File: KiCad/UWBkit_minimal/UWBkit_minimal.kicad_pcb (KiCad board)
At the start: 2 copper layers, 49 x 39.1 mm, 57 parts, among them J1 Conn_UART, J2 Conn_SWD, J3 USB_C_Receptacle_USB2.0_14P, J4 Conn_BATT, J5 Jumper_Cell_NO, Q1 BSS138, Q2 BSS138, Q3 BSS84, SW1 SW_Push, U1 DWM3001C, U2 IP4234CZ6, U3 MAX40203AUK+T, U4 XC9285B33CMR-G

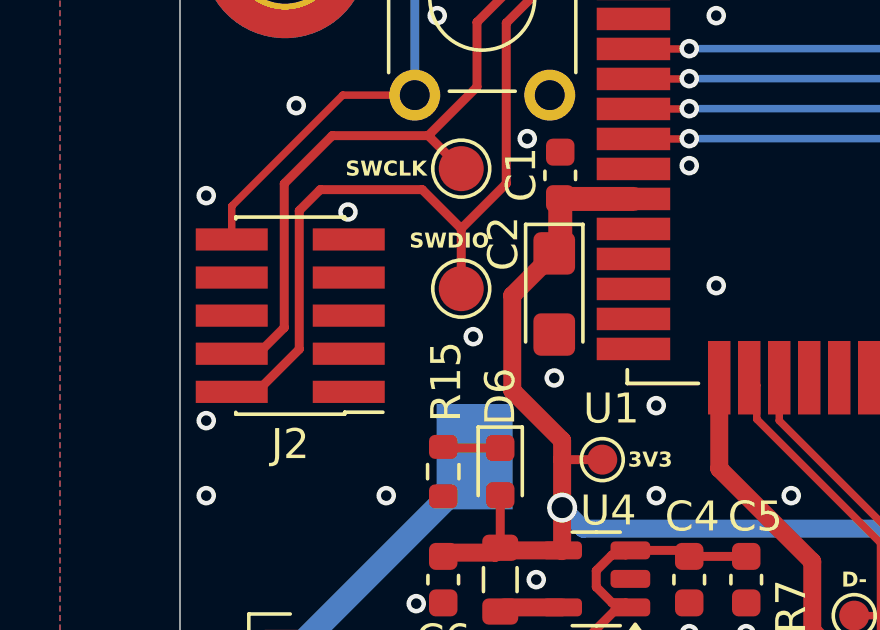
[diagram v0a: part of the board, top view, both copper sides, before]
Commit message: Fixed a missing connection to JTAG
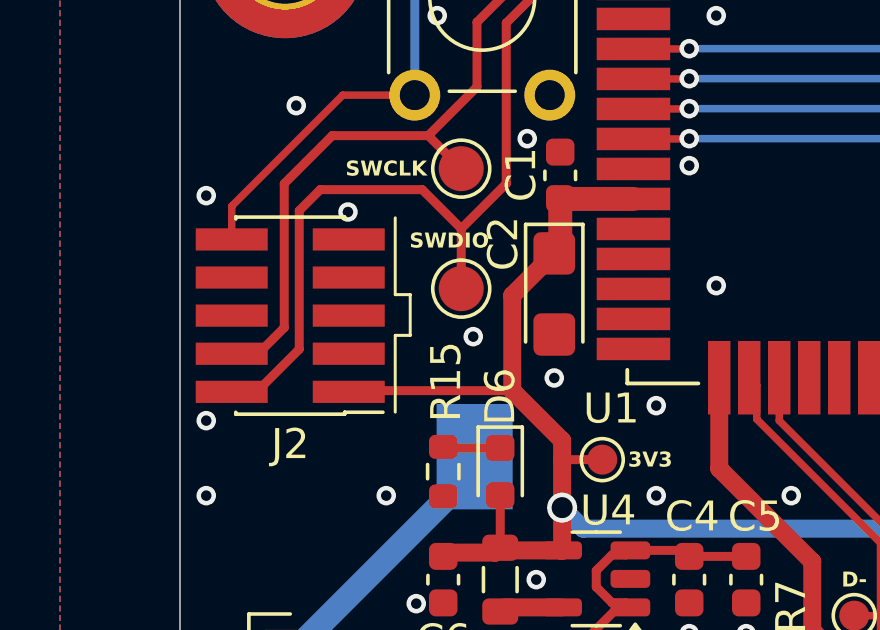
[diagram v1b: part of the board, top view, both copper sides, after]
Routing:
- net +3V3: track 75.7 -> 81.2 mm
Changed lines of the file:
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@@
 			(psa4output no)
 			(plot_black_and_white yes)
-			(plotinvisibletext no)
 			(sketchpadsonfab no)
 			(plotpadnumbers no)
@@
 	)
 	(gr_line
+		(start 134.3 77.3)
+		(end 134.3 74.74)
+		(stroke
+			(width 0.1)
+			(type default)
+		)
+		(layer "F.SilkS")
+	)
+	(gr_line
+		(start 134.3 78.657121)
+		(end 134.8 78.657121)
+		(stroke
+			(width 0.1)
+			(type default)
+		)
+		(layer "F.SilkS")
+	)
+	(gr_line
+		(start 134.8 78.657121)
+		(end 134.8 77.3)
+		(stroke
+			(width 0.1)
+			(type default)
+		)
+		(layer "F.SilkS")
+	)
+	(gr_line
+		(start 134.3 81.217121)
+		(end 134.3 78.657121)
+		(stroke
+			(width 0.1)
+			(type default)
+		)
+		(layer "F.SilkS")
+	)
+	(gr_line
+		(start 134.8 77.3)
+		(end 134.3 77.3)
+		(stroke
+			(width 0.1)
+			(type default)
+		)
+		(layer "F.SilkS")
+	)
+	(gr_line
 		(start 151.625 96.6)
 		(end 151.625 106.6)
@@
 	)
 	(segment
+		(start 132.79 80.5)
+		(end 132.75 80.54)
+		(width 0.3)
+		(layer "F.Cu")
+		(net 2)
+	)
+	(segment
 		(start 139.8625 85.85)
 		(end 139.8375 85.825)
@@
 		(width 0.3)
 		(layer "F.Cu")
+		(net 2)
+	)
+	(segment
+		(start 138.2 80.5)
+		(end 132.79 80.5)
+		(width 0.3)
+		(layer "F.Cu")
